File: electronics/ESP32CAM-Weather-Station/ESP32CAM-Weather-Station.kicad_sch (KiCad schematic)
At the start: 0 parts

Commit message: [WIP] Included libraries and setup board.
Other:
- company: (none) -> Ilias Kringos (ilkringos@gmail.com)
- title: (none) -> ESP32CAM-Weather-Station
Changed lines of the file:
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@@
 	(generator "eeschema")
 	(generator_version "9.0")
-	(paper "A4")
+	(paper "A3")
+	(title_block
+		(title "ESP32CAM-Weather-Station")
+		(company "Ilias Kringos (ilkringos@gmail.com)")
+	)
 	(sheet_instances
 		(path "/"

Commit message: [WIP] Placed basic parts.
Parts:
- added D1, D2: LED_RED, LED_SMD:LED_0805_2012Metric_Pad1.15x1.40mm_HandSolder, symbol Device:LED
- added F1: SF-1206FP400-2, SF-1206FP400-2:FUSC3116X70N, symbol SF-1206FP400-2:SF-1206FP400-2
- added F2: MF-USHT125KX_12-2, MF-USHT125KX_12-2:MFUSHT125KX122, symbol MF-USHT125KX_12-2:MF-USHT125KX_12-2
- added H1: 12BHC186P2-GR, 12BHC186P2-GR:12BHC186P2GR, symbol 12BHC186P2-GR:12BHC186P2-GR
- added IC1: BME688, BME688:BME688, symbol BME688:BME688
- added IC2: SGP41-D-R4, SGP41-D-R4:SON80P244X244X95-7N, symbol SGP41-D-R4:SGP41-D-R4
- added IC3: VEML7700-TT, VEML7700-TT:VEML7700, symbol VEML7700-TT:VEML7700-TT
- added IC4: BQ24093DGQR, BQ24093DGQR:SOP50P490X110-11N, symbol BQ24093DGQR:BQ24093DGQR
- added IC5: BQ29707DSET, BQ29707DSET:TPS610985DSET, symbol BQ29707DSET:BQ29707DSET
- added IC6: MCP3426A0T-E_SN, MCP3426A0T-E_SN:SOIC127P600X175-8N, symbol MCP3426A0T-E_SN:MCP3426A0T-E_SN
- added IC7: TPS63070RNMR, TPS63070RNMR:TPS630701RNMR, symbol TPS63070RNMR:TPS63070RNMR
- added J1, J2, J3, J4, J5: B4B-PH-SM4-TB_LF__SN_, B4B-PH-SM4-TB_LF__SN_:B4B-PH-SM4_1, symbol B4B-PH-SM4-TB_LF__SN_:B4B-PH-SM4-TB_LF__SN_
- added J6: XT30UPB-M, XT30UPB-M:AMASS_XT30UPB-M, symbol XT30UPB-M:XT30UPB-M
- added LS1: CMT-7525-80-SMT-TR, CMT-7525-80-SMT-TR:CMT752580SMTTR, symbol CMT-7525-80-SMT-TR:CMT-7525-80-SMT-TR
- added Q1: SIHLL110TR-GE3, SIHLL110TR-GE3:SOT230P700X180-4N, symbol SIHLL110TR-GE3:SIHLL110TR-GE3
- added R1, R2: 1k, Resistor_SMD:R_0805_2012Metric_Pad1.20x1.40mm_HandSolder, symbol Device:R
- added S1: TS18-5-25-SL-260-SMT-TR, TS18-5-25-SL-260-SMT-TR:TS18525SL260SMTTR, symbol TS18-5-25-SL-260-SMT-TR:TS18-5-25-SL-260-SMT-TR
- added U1: ESP32-CAM, ESP32-CAM:ESP32-CAM, symbol ESP32-CAM:ESP32-CAM
- added U2: TPS631000DRLR, SOTFL50P160X60-8N, symbol TPS631000DRLR:TPS631000DRLR
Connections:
- new net: D2.1 (K), R2.1
- new net: D1.1 (K), R1.1
- new net: F1.1, H1.1 (+)
- new net: F2.2, U2.1 (VOUT)
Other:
- note added: "3.3V Supply"
- note added: "BME688 (T,H,P,G)"
- note added: "Battery Charging"
- note added: "Battery Management and Input"
- note added: "Battery and Solar Supply Sense ADC"
- note added: "Battery and Solar Supply Voltage Dividers"
- note added: "ESP32-CAM"
- note added: "External Sensors/Hardware"
- note added: "Indicators"
- note added: "Reset Button"
- note added: "SGP41 (NOx, VOC)"
- note added: "Solar Input"
- note added: "VEML7700 (Lux)"

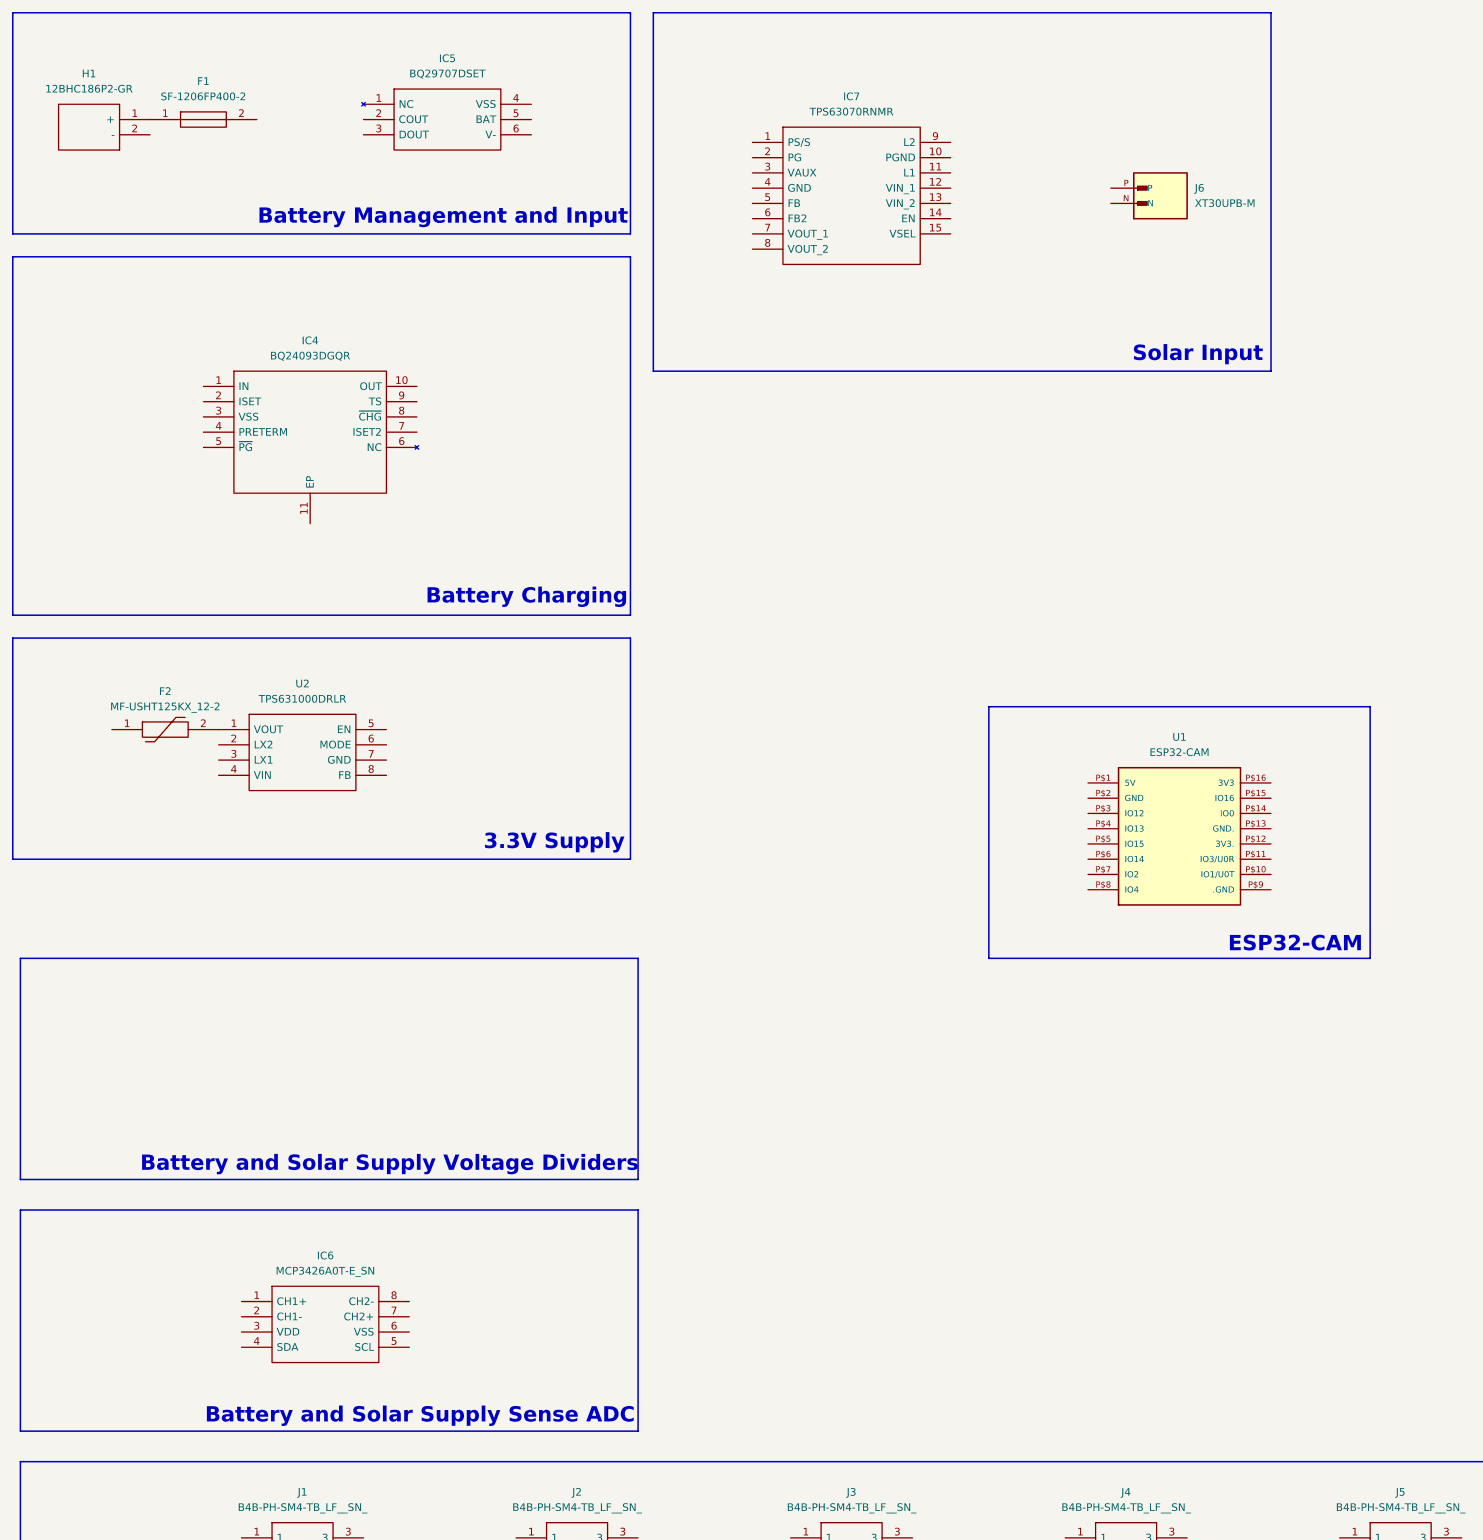
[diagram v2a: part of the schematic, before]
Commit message: [WIP] Added battery access header, I2C pullups and ADC voltage dividers.
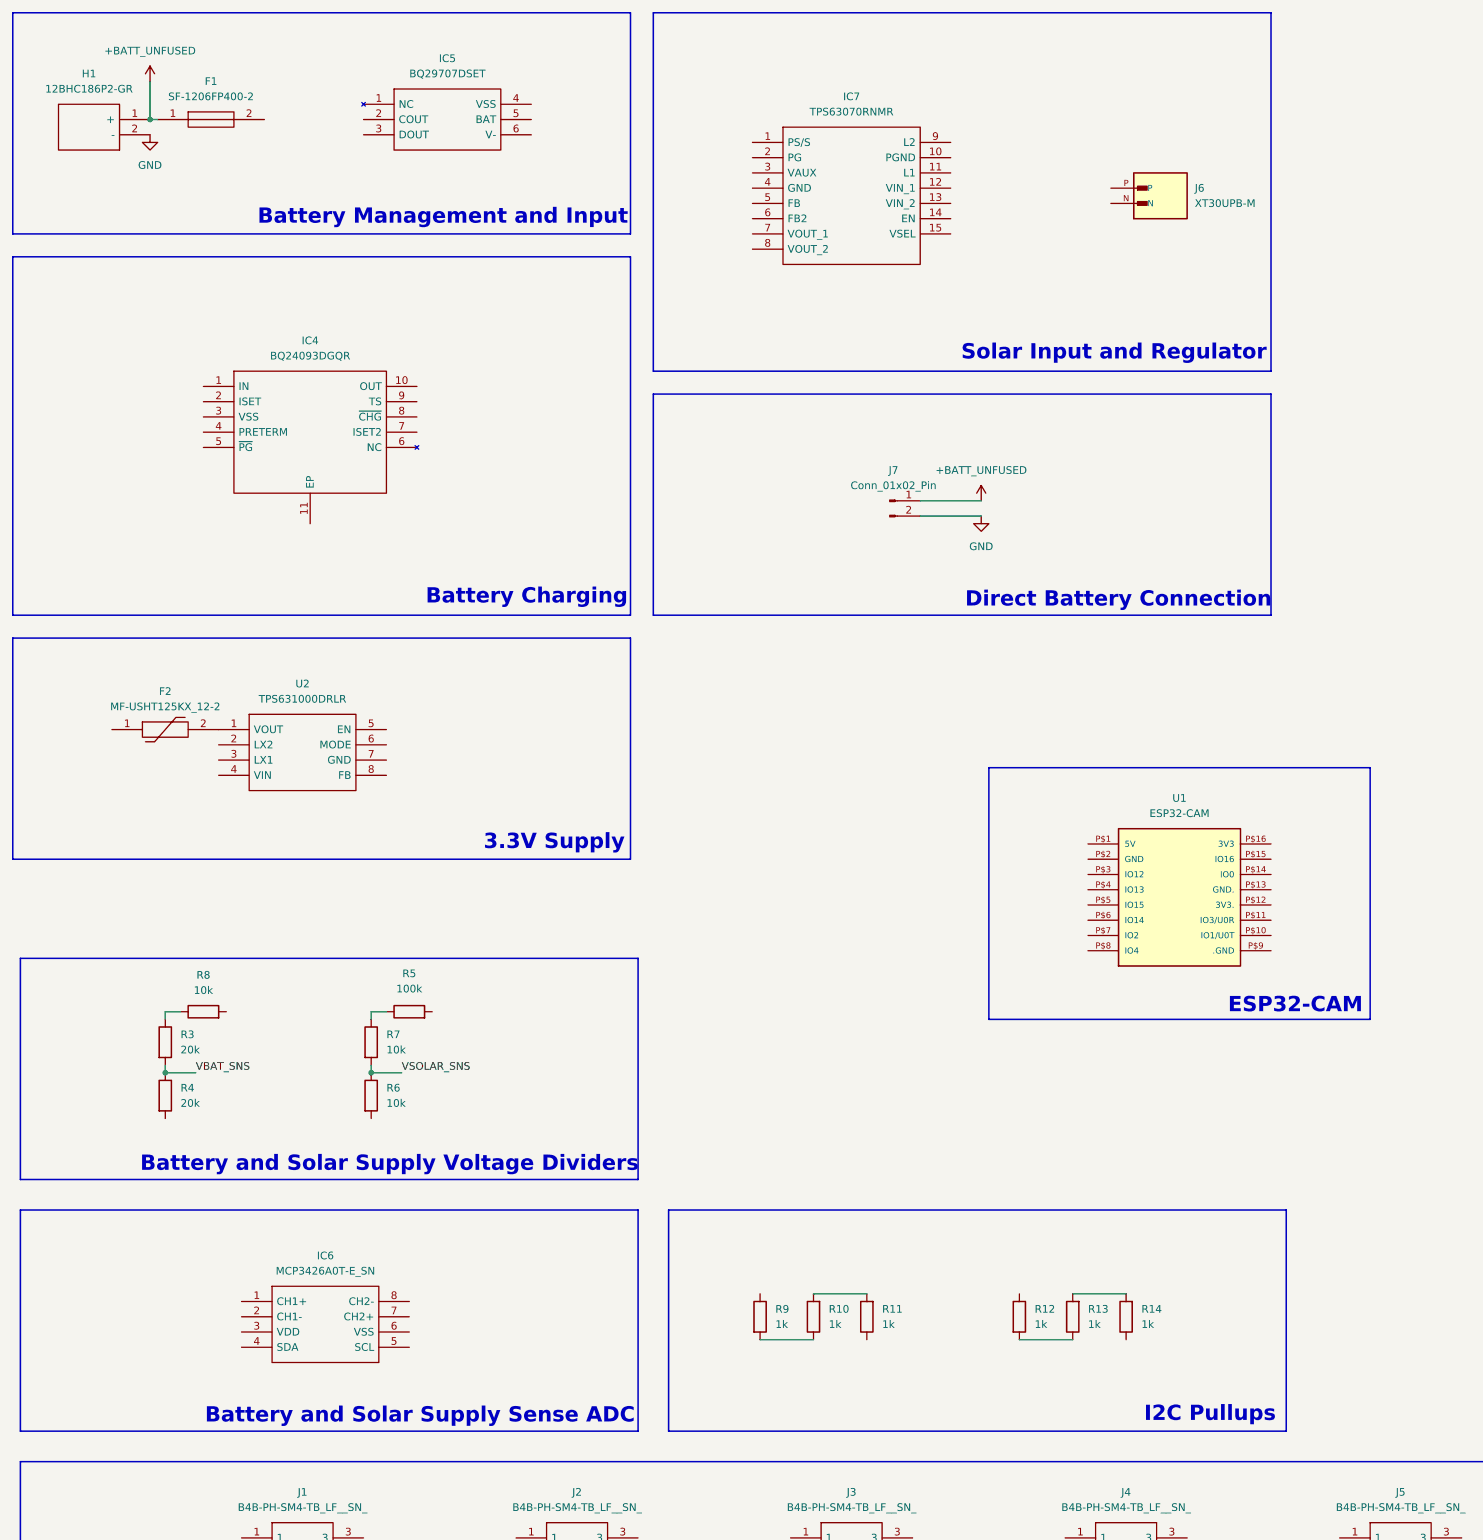
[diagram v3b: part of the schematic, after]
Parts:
- added J7: Conn_01x02_Pin, Connector_PinHeader_2.54mm:PinHeader_1x02_P2.54mm_Vertical, symbol Connector:Conn_01x02_Pin
- added R10, R11, R12, R13, R14, R9: 1k, Resistor_SMD:R_0805_2012Metric_Pad1.20x1.40mm_HandSolder, symbol Device:R
- added R3, R4: 20k, Resistor_SMD:R_0805_2012Metric_Pad1.20x1.40mm_HandSolder, symbol Device:R
- added R5: 100k, Resistor_SMD:R_0805_2012Metric_Pad1.20x1.40mm_HandSolder, symbol Device:R
- added R6, R7, R8: 10k, Resistor_SMD:R_0805_2012Metric_Pad1.20x1.40mm_HandSolder, symbol Device:R
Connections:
- net +BATT_UNFUSED: now reaches F1.1, H1.1 (+)
- net +BATT_UNFUSED: now also J7.1 (Pin_1)
- net GND: now reaches H1.2 (-)
- net GND: now also J7.2 (Pin_2)
- new net: R12.2, R13.1
- new net: R5.1, R7.1
- new net: R13.2, R14.2
- new net: R3.1, R8.1
- new net: R10.1, R9.2
- new net: R10.2, R11.2
- new net VBAT_SNS: R3.2, R4.1
- new net VSOLAR_SNS: R6.1, R7.2
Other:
- note added: "Direct Battery Connection"
- note added: "I2C Pullups"
- note added: "Solar Input and Regulator"
- note removed: "Solar Input"
- moved on the sheet: F1, U1

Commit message: [WIP] Added ESP32-CAM, I2C Pullup, JST Connections.
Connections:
- net GND: now also J1.2, J2.2, J3.2, J4.2, J5.2, R4.2, R6.2, U1.P$13 (GND.), U1.P$2 (GND), U1.P$9 (.GND)
- net +3.3V: now reaches R12.1
- net +3.3V: now also J1.1, J2.1, J3.1, J4.1, J5.1, R9.1, U1.P$16 (3V3)
- net I2C_SCL: now reaches J1.3
- net I2C_SCL: now also J2.3, J3.3, R14.1, U1.P$11 (IO3/U0R)
- net I2C_SDA: now reaches J1.4
- net I2C_SDA: now also J2.4, J3.4, R11.1, U1.P$15 (IO16)
- net GPIO1: now reaches U1.P$10 (IO1/U0T)
- net GPIO1: now also J4.4, J5.4
- net GPIO0: now reaches U1.P$14 (IO0)
- net GPIO0: now also J4.3, J5.3
- no-connect marks 0 -> 8
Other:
- moved on the sheet: R3, R4, R5, R6, R7, R8

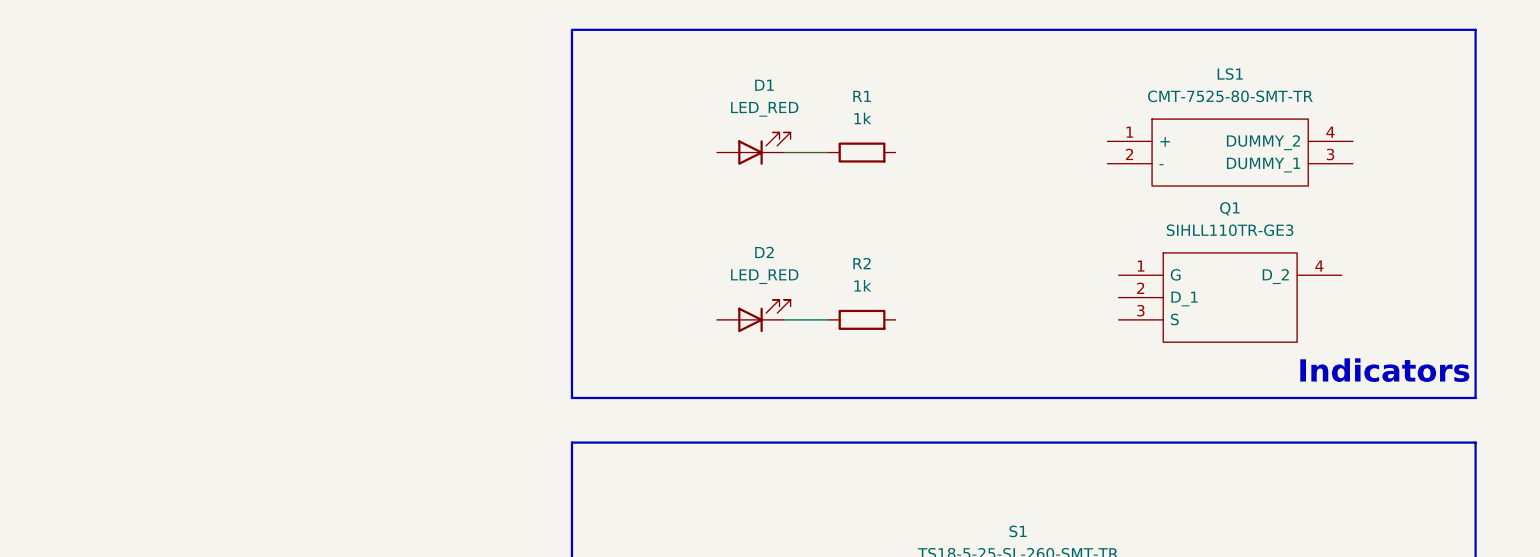
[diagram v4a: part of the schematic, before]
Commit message: [WIP] Connected GPIO pins to LEDs, Buzzer.
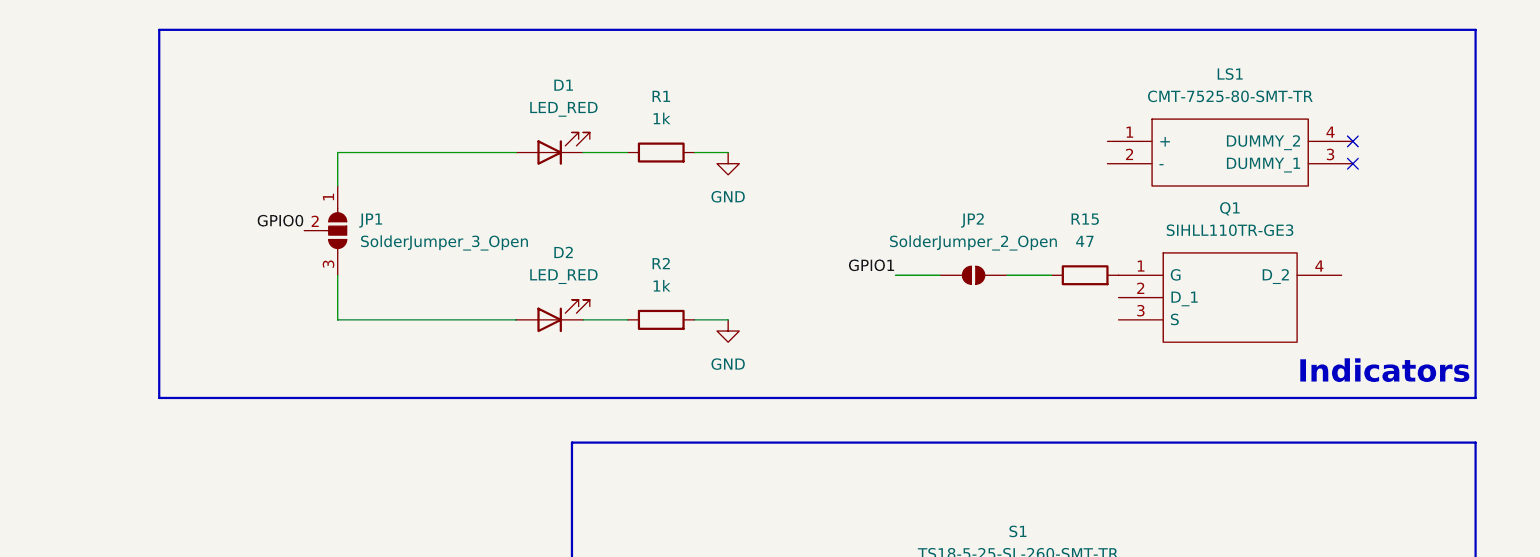
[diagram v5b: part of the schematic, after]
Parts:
- added JP1: SolderJumper_3_Open, symbol Jumper:SolderJumper_3_Open
- added JP2: SolderJumper_2_Open, symbol Jumper:SolderJumper_2_Open
- added R15: 47, Resistor_SMD:R_0805_2012Metric_Pad1.20x1.40mm_HandSolder, symbol Device:R
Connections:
- net GND: now also R1.2, R2.2
- net GPIO0: now also JP1.2 (C)
- net GPIO1: now also JP2.1 (A)
- net at D1.2 (A): now also JP1.1 (A)
- net at Q1.1 (G): now also R15.2
- net at D2.2 (A): now also JP1.3 (B)
- new net: JP2.2 (B), R15.1
- no-connect marks 8 -> 10
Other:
- moved on the sheet: D1, D2, R1, R2
